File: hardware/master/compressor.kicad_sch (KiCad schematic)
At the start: 119 parts, among them SW401 COMP ON (latching), U401 SSI2162, U402 AS3046D, U403 NE5532, U404 NE5532, U405 NE5532, U406 TL072, U407 TL072, U408 TL072, U409 TL072, U410 TL072, U411 LM339, U412 LM339, U413 DG413DY

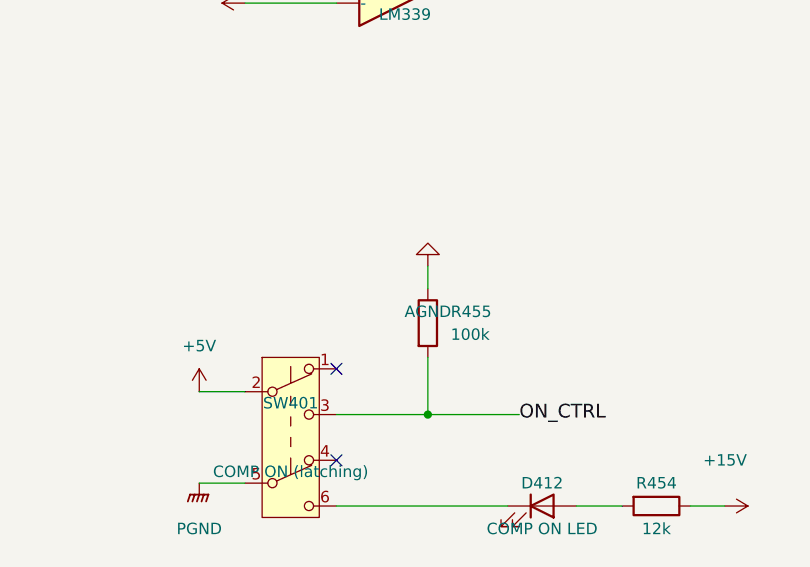
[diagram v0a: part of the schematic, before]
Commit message: Master card: draw decisions 97 and 98, OPA2171 fader-law stages (103), SC_ENV drive (104)
- AUX returns: SC_ENV into the summer's virtual earth through R232/R332 30k1,
  R233/R333 removed, summer + input on AGND (decision 97)
- Q501 emitter and button pull-downs R237/239/241, R337/339/341, R455,
  R523/525/527 to PGND (decision 98)
- U206, U306, U705 = OPA2171 for the pot buffer and control summer; superdiodes
  on the TL072s U207, U307, U706 (decision 103)
- Sidechain: DEPTH negative (R518 to -15 V), U505B follower fed back after R521,
  D504 BAT54T1G clamp to AGND (decision 104); simulation rerun with 1.7 kOhm load
- R421 on its 0603 footprint (system validation finding 3)
- Power budget, parts list, STATUS, decisions and working notes updated

Co-Authored-By: Claude Opus 5.5 <noreply@anthropic.com>
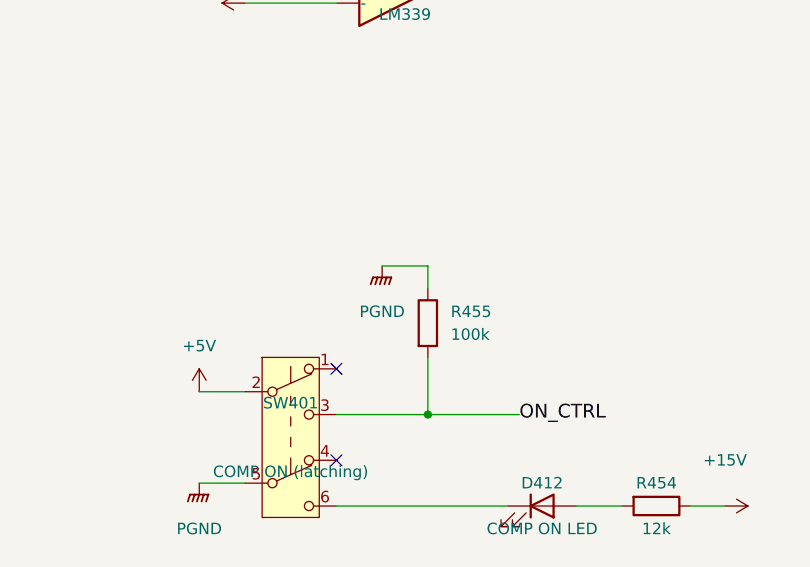
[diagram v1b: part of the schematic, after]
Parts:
- R421: footprint Resistor_SMD:R_0805_2012Metric -> Resistor_SMD:R_0603_1608Metric
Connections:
- net AGND: no longer R455.1
- net PGND: now also R455.1

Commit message: Master card: DRV135 outputs, TL062 levers, SMD electrolytics, both raw rails watched (decisions 125-128)
/board master pre-layout session; the user delegated the open points.
- Confirms the [proposed] parts of decisions 89-94 (Q5 checked, +22 dB
  makeup kept for the breadboard, fallback R439 = 330k).
- 125: TI DRV135UA replaces the end-of-life THAT1646 (THAT memo
  2026-09-01); same SO-8 pinout, LCSC C544663.
- 126: U409, U410, U802, U804 TL072 -> TL062; superdiodes and U407 stay.
- 127: master electrolytics to SMD (decision 111 parts, 5.4 mm).
- 128: U707C watches -20V_RAW (22k6/100k), wired-OR with the +20 V trip.
- Würth fields on J101/J901, BAT54 LCSC C152458, G6K and header
  drawings checked, LCSC stock checked; budget 331/260 mA typical.
- parts.csv candidates for master pots and meter LEDs; lcsc_check.py
  handles MOhm.
ERC 0/0, all netlist checks 0 problems, reuse lint clean.

Co-Authored-By: Claude Opus 5.5 <noreply@anthropic.com>
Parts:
- removed U409, U410: TL072, Package_SO:SOIC-8_3.9x4.9mm_P1.27mm, symbol Amplifier_Operational:TL072
- added U409, U410: TL062, Package_SO:SOIC-8_3.9x4.9mm_P1.27mm, symbol Amplifier_Operational:TL062
- C401, C402: footprint Capacitor_THT:C_Radial_D5.0mm_H11.0mm_P2.00mm -> Capacitor_SMD:C_Elec_6.3x5.4; MPN (none) -> EEE-1VA100NP; Manufacturer (none) -> Panasonic; ProjectPN SX-C-003 -> SX-C-023; Supplier (none) -> Mouser; SupplierPN (none) -> 667-EEE-1VA100NP
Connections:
- net +15V: now also U409.8 (V+), U410.8 (V+)
- net -15V: now also U409.4 (V-), U410.4 (V-)
- net AGND: now also U409.3 (+), U409.5 (+), U410.3 (+)
- net GRP: now also U410.1
- net VAMT: now also U410.6 (-), U410.7
- net VC: now also U409.7
- net at D406.1 (K), R429.2, R430.2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: now also U409.2 (-)
- net at C411.1, R436.2, R438.2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: now also U409.6 (-)
- net at C409.1, R427.2, R428.1: now also U410.5 (+)
- net at R441.2, R442.1: now also U410.2 (-)
- net at D405.1 (K), D406.2 (A): now also U409.1

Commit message: Master card: RELEASE pot C100K for Alpha's 0.02 W rating (decision 131)
- RV402 C10K -> C100K (Alpha RD901F-40-15K-C100K, Tayda A-5370,
  SX-POT-014), R425 620R -> 6k2 (SX-R-091): about 2 mW instead of
  20 mW; only the R425/track ratio sets the law
- Simulated release 44 / 353 / 1427 ms per 10 dB (was 44 / 351 /
  1422 ms); raising R425 alone would have cut the CW end to ~0.3 s
- run.py takes the pot value; parts, STATUS, index updated
- hardware/CLAUDE.md: Tayda blocks scripts; check decision and SX
  numbers across worktrees before numbering

Netlists match, ERC 0/0.

Co-Authored-By: Claude Opus 5.5 <noreply@anthropic.com>
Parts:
- R425: value 620 -> 6k2; ProjectPN SX-R-057 -> SX-R-091
- RV402: value RELEASE 10k rev. log -> RELEASE 100k rev. log; MPN (none) -> RD901F-40-15K-C100K; Manufacturer (none) -> Alpha; Note Panel RELEASE: reverse-log (C) taper, CCW = 44 ms, CW = 1.4 s per 10 dB -> Panel RELEASE: reverse-log (C) taper, CCW = 44 ms, CW = 1.4 s per 10 dB; 100k keeps it at about 2 mW (Alpha non-B rating 0.02 W, decision 131); ProjectPN SX-POT-004 -> SX-POT-014; Supplier (none) -> Tayda; SupplierPN (none) -> A-5370

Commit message: Master card: fee-free parts and E24 values (decisions 144, 146-150)
- 144: AUX return and master fader laws on the channel's E24 pairs
- 146: meter ladder on fee-free E24 values (0.45 mA, within 0.14 dB); R732 22k + R737 560R
- 147: compressor R420/R426 E24 pairs, GR LED ladder 470k/4k3, SC LPF C503 2 x 47n C0G
  (Q 0.707, 44-478 Hz); TL072 symbols ST TL072CDT
- 148: AUX return receivers TL072 difference amplifiers (AD8273 gone from the project)
- 149: R421 plain 1k; compressor temperature compensation to the backlog
- 150: DG413, SSI2162, DRV135UA, AS3046D hand-soldered on the prototype master
  (symbol field Assembly, read by tools/costs.py); SPOF noted in the backlog
- Part swaps: button LEDs per colour, D504 BAT54W, D705-D712 1N4007W SOD-123FL,
  U641 DG411 -> DG413 with a Q601 inverter for send 1 (emitter on PGND, invariant 4)
- 70 -> 38 extended/consigned SMD types (about EUR 193 -> 105 per order);
  estimate EUR 794 / 1,074 / 1,671 for 4 / 8 / 16 channels
- Docs: STATUS, CONTINUE-FROM-HERE, ROADMAP backlog, SPEC, hardware/CLAUDE.md lessons

Co-Authored-By: Claude Opus 5.5 <noreply@anthropic.com>
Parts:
- added R456: 51k, Resistor_SMD:R_0805_2012Metric, symbol Device:R
- added R457: 20k, Resistor_SMD:R_0805_2012Metric, symbol Device:R
- D412: MPN (none) -> KT-0805G; Manufacturer (none) -> Hubei KENTO; ProjectPN SX-D-002 -> SX-D-011; Supplier (none) -> LCSC; SupplierPN (none) -> C2297
- R420: value 560k -> 510k; ProjectPN SX-R-053 -> SX-R-114
- R421: value 1k +3300 ppm/K -> 1k; footprint Resistor_SMD:R_0603_1608Metric -> Resistor_SMD:R_0805_2012Metric; MPN ERA-V33J102V -> (none); Manufacturer Panasonic -> (none); Note Place against U402 (AS3046D) for thermal tracking -> Plain 1k on the prototype (decision 149); temperature compe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; ProjectPN SX-R-021 -> SX-R-035
- R426: value 140k -> 120k; ProjectPN SX-R-058 -> SX-R-115
- R443: value 453k -> 470k; ProjectPN SX-R-024 -> SX-R-048
- R445: value 4k02 -> 4k3; ProjectPN SX-R-038 -> SX-R-113
- U401, U402, U413: Assembly (none) -> hand (decision 150)
- U406, U407, U408: MPN (none) -> TL072CDT; Manufacturer Texas Instruments -> STMicroelectronics; Supplier (none) -> LCSC; SupplierPN (none) -> C6961
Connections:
- net +15V: now also R456.1, R457.2; no longer R420.1, R426.2
- new net: R420.1, R456.2
- new net: R426.2, R457.1

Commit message: Buttons: SX-SW-001 is the latching GPBS850L, not the momentary GPBS850N
Electrokit 41012905 (on-on, latching) links the GPBS850N datasheet, which
is the momentary twin (Electrokit 41015527, Mouser "Non-Latching ON-(ON)");
the MPN was copied from that file. The latching part is CW GPBS850L
(datasheet Rev 2, 2014: same body, pin grid and pressed = 2-3, 5-6 contacts;
plunger 4.0 mm instead of 3.8).

MPN and footprint name corrected on all 17 button symbols, the generator
scripts and the input reference; parts.csv gets the GPBS850L datasheet and
RoHS source (Mouser 629-GPBS-850L, DigiKey CW179-ND); prices.csv gets the
Electrokit price (6.48 SEK ex VAT at 25+). Erratum on decision 75, checklist
item for the delivered switches and cap sizing, correction notes in the
RoHS audit and the cost review. No wiring change; ERC 0/0 on both cards.
Estimate €769 / €1,037 / €1,609 for 4 / 8 / 16 channels.

Co-Authored-By: Claude Opus 5.5 <noreply@anthropic.com>
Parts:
- SW401: footprint syntsamix:SW_Latching_8.5x8.5mm_CW_GPBS850N -> syntsamix:SW_Latching_8.5x8.5mm_CW_GPBS850L; MPN GPBS850N -> GPBS850L
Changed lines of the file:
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@@
 			)
 		)
-		(property "Footprint" "syntsamix:SW_Latching_8.5x8.5mm_CW_GPBS850N"
+		(property "Footprint" "syntsamix:SW_Latching_8.5x8.5mm_CW_GPBS850L"
 			(at 439.42 236.22 0)
 			(hide yes)
@@
 			)
 		)
-		(property "MPN" "GPBS850N"
+		(property "MPN" "GPBS850L"
 			(at 439.42 236.22 0)
 			(hide yes)

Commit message: Master: headphone jack, 0805 LEDs, off-board parts in the estimate (decisions 169-171)
- J751 becomes a KK 1x3 header for the panel Rean NYS230 with a ready-made
  Molex 217797-1031 lead (169)
- Master meter, gain-reduction (yellow) and PFL-active LEDs all 0805 basic
  parts; SX-D-005/006 retired (170)
- tools/costs.py counts parts without a schematic symbol from
  docs/costs/offboard.csv, and the two rear row-board PCBs (171):
  estimate EUR 831 / 1,110 / 1,693 for 4 / 8 / 16 channels
- New parts SX-CONN-019..022; ready-made input-module cable noted for /system
- NYS216/NYS230 samples to order; heatsink choice on hold (none fits 25 mm
  at decision 167's 57 C air), options in master STATUS

Co-Authored-By: Claude Opus 5.5 <noreply@anthropic.com>
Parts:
- D407, D408, D409, D410, D411: footprint LED_THT:LED_D3.0mm -> LED_SMD:LED_0805_2012Metric; MPN (none) -> KT-0805Y; Manufacturer (none) -> Hubei KENTO; Note Gain-reduction LED; colour to confirm -> Gain-reduction LED, 0805 under a printed bezel (decision 16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; ProjectPN SX-D-005 -> SX-D-016; Supplier (none) -> LCSC; SupplierPN (none) -> C2296

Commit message: Master: back-to-back coupling pairs, ten NE5532 to TL072, Wakefield heatsinks, onsemi TO-220 regulators (decisions 172-174)
Co-Authored-By: Claude Opus 5.5 <noreply@anthropic.com>
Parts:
- removed C401, C402: 10u bipolar, Capacitor_SMD:C_Elec_6.3x5.4, symbol Device:C
- removed U403, U404, U405: NE5532, Package_SO:SOIC-8_3.9x4.9mm_P1.27mm, symbol Amplifier_Operational:NE5532
- added C401, C402, C432, C433: 10u 35V, Capacitor_SMD:CP_Elec_5x5.4, symbol Device:C_Polarized
- added U403, U404, U405: TL072, Package_SO:SOIC-8_3.9x4.9mm_P1.27mm, symbol Amplifier_Operational:TL072
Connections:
- net +15V: now also U403.8 (V+), U404.8 (V+), U405.8 (V+)
- net -15V: now also U403.4 (V-), U404.4 (V-), U405.4 (V-)
- net AGND: now also U403.3 (+), U403.5 (+), U404.3 (+), U404.5 (+)
- net COMP_L_SUM: now also C401.1
- net COMP_R_SUM: now also C402.1
- net DRY_L: now also U404.1
- net DRY_R: now also U404.7
- net L_MIXW: now also U405.3 (+)
- net R_MIXW: now also U405.5 (+)
- net WET_L: now also U403.1
- net WET_R: now also U403.7
- net at C405.1, R406.1, U401.4 (IOUT1): now also U403.2 (-)
- net at R402.1: now also C433.1
- net at R410.2, R411.1: now also U404.6 (-)
- net at R401.1: now also C432.1
- net at R412.1: now also U405.1, U405.2 (-)
- net at R413.1: now also U405.6 (-), U405.7
- net at C406.1, R407.1, U401.7 (IOUT2): now also U403.6 (-)
- net at R408.2, R409.1: now also U404.2 (-)
- new net: C401.2, C432.2
- new net: C402.2, C433.2
